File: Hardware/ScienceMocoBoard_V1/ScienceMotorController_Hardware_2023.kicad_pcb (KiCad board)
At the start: 2 copper layers, 231.4 x 127 mm, 136 parts, among them Q1 SI4156DY, Q10 SI4156DY, Q11 SI4156DY, Q12 SI4156DY, Q13 SI4156DY, Q14 SI4156DY, Q15 SI4156DY, Q16 SI4156DY, Q2 SI4156DY, Q3 SI4156DY, Q4 SI4156DY, Q5 SI4156DY, Q6 SI4156DY, Q7 SI4156DY, Q8 SI4156DY, Q9 SI4156DY, U1 IRS2005S, U10 IRS2005S, U11 TM4C129E_Launchpad, U2 IRS2005S, U3 3V3 OKI, U4 TSR_1-2450, U5 IRS2005S, U6 IRS2005S, U7 IRS2005S, U8 IRS2005S, U9 IRS2005S

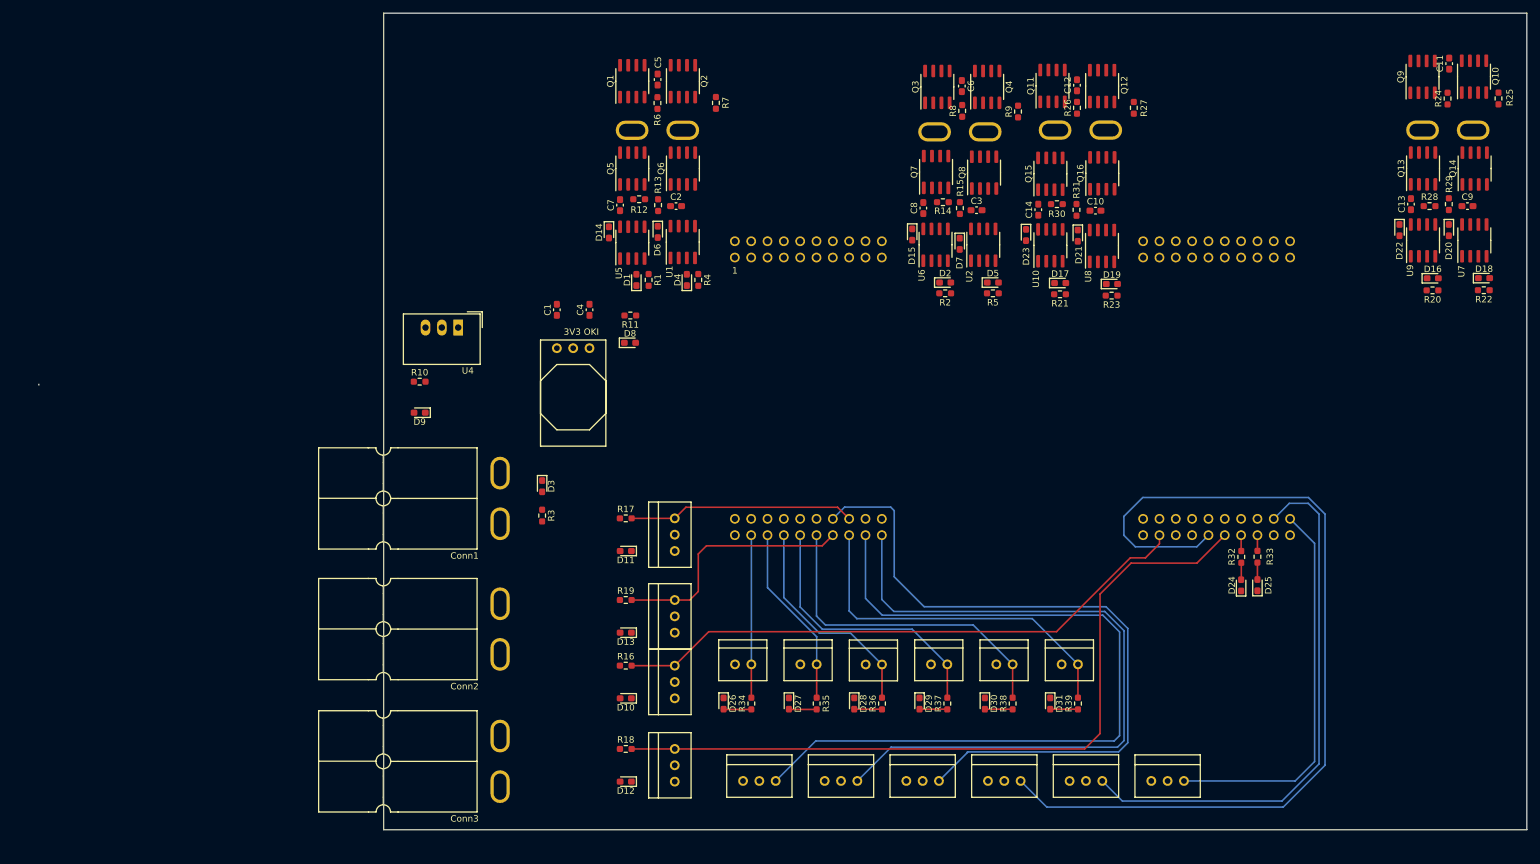
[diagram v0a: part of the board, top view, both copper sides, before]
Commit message: Rearranged Board. Traced Power and One H-Bridge
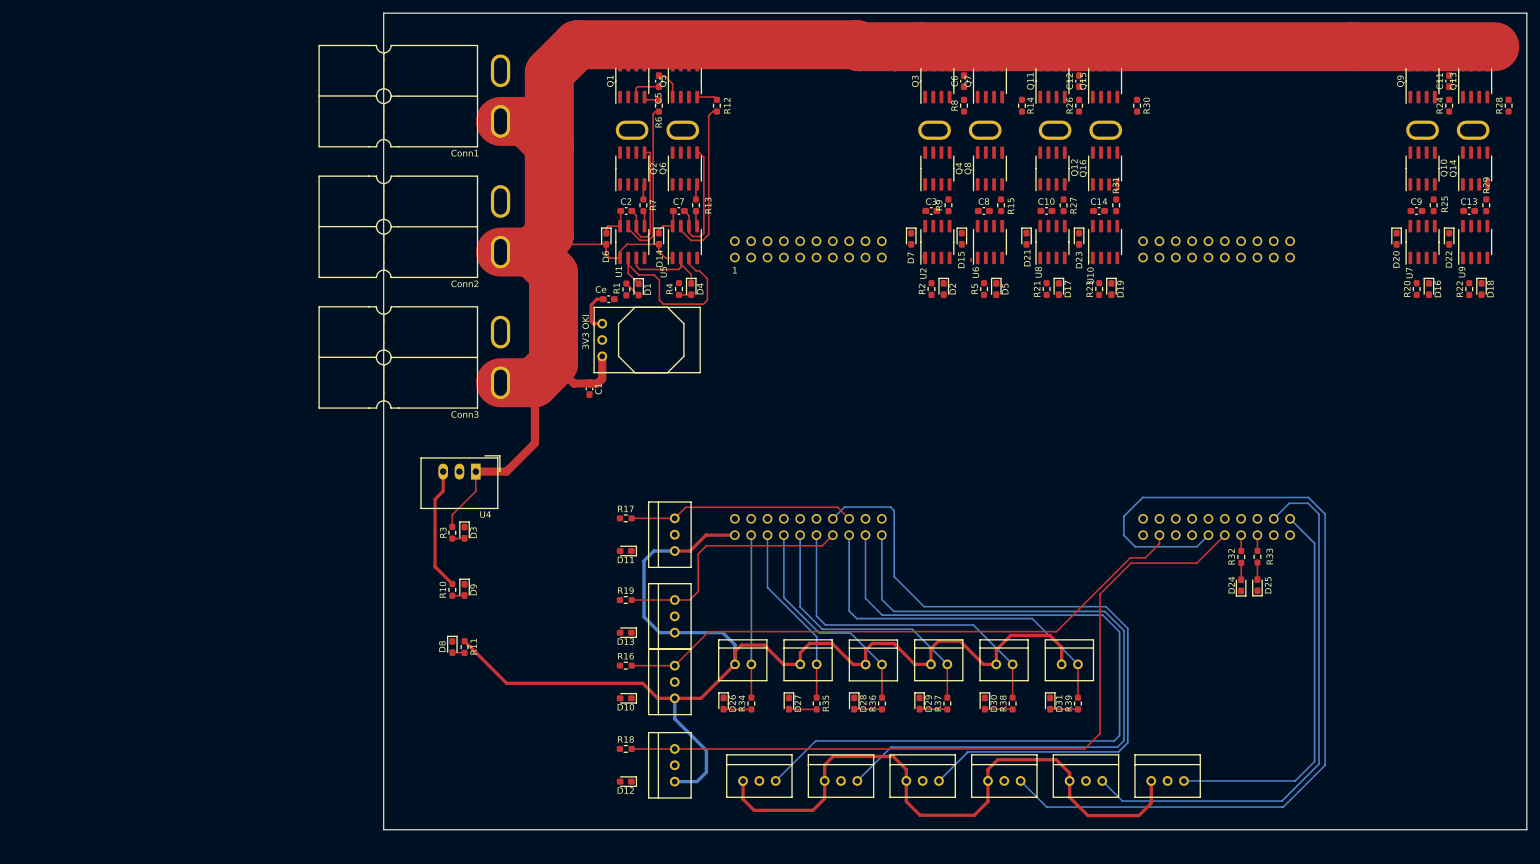
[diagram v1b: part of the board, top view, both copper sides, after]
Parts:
- moved Conn3 62.8 mm to (82.8, 74.9)
- moved Conn2 62.6 mm to (82.8, 54.6)
- moved Conn1 62.6 mm to (82.8, 34.3)
- moved R11 57.6 mm to (76.8, 124.5), turned to 90 degrees
- moved D8 54.8 mm to (74.9, 124.5), turned to -90 degrees
- moved R10 32.8 mm to (74.9, 115.6), turned to 90 degrees
- moved D9 28.4 mm to (76.8, 115.6), turned to -90 degrees
- moved U4 22.6 mm to (78.6, 97.2)
- moved R28 19.9 mm to (239.2, 40.3), turned to 90 degrees
- moved R30 19.8 mm to (181.4, 40.3), turned to 90 degrees
- moved R7 19.5 mm to (104.6, 55.8)
- moved R25 19.4 mm to (227.6, 55.8)
- moved R14 19.4 mm to (163.5, 40.3), turned to 90 degrees
- moved R12 18.9 mm to (116.1, 40.3), turned to 90 degrees
- moved R27 18.7 mm to (170.0, 55.8)
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- renumbered C4 to Ce
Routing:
- net +12V: track 0.00 -> 299.0 mm
- net +3V3: track 0.00 -> 190.6 mm
- net +5V: track 0.36 -> 116.4 mm
- net FWD_PWM_1: track 0.00 -> 30.7 mm
- net Net-(R12-Pad1): track 0.00 -> 26.0 mm
- net Net-(R6-Pad1): track 0.00 -> 25.3 mm
- net /M+: track 0.00 -> 24.7 mm
- net /M-: track 0.00 -> 24.3 mm
- net RVS_PWM_1: track 0.00 -> 14.6 mm
- net Net-(C2-Pad1): track 0.00 -> 5.46 mm
- net Net-(C7-Pad1): track 0.00 -> 5.27 mm
- net Net-(Q5-Pad4): track 0.00 -> 3.25 mm
- net Net-(D1-Pad2): track 0.00 -> 2.65 mm
- net Net-(Q1-Pad4): track 0.00 -> 2.41 mm
- net Net-(R7-Pad1): track 0.00 -> 2.40 mm
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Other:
- board size 231.4 x 127 mm -> 177.8 x 127 mm

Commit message: More tracing. Ground is left.
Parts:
- moved AbsEncode4 1.17 mm to (109.5, 133.6)
- moved D15 0.43 mm to (154.6, 61.0)
- moved C11 0.38 mm to (230.0, 36.8)
- moved C12 0.38 mm to (172.4, 36.8)
- moved C6 0.38 mm to (154.5, 36.8)
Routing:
- net +12V: track 299.0 -> 432.1 mm
- net +5V: track 116.4 -> 205.7 mm
- net RVS_PWM_2: track 0.00 -> 81.7 mm
- net FWD_PWM_2: track 0.00 -> 81.5 mm
- net FWD_PWM_3: track 0.00 -> 77.5 mm
- net /M+: track 24.7 -> 98.6 mm
- net /M-: track 24.3 -> 93.8 mm
- net RVS_PWM_3: track 0.00 -> 62.3 mm, vias 0 -> 2
- net FWD_PWM_4: track 0.00 -> 55.4 mm
- net RVS_PWM_4: track 0.00 -> 53.8 mm, vias 0 -> 2
- net +3V3: track 190.6 -> 232.1 mm
- net RVS_PWM_1: track 14.6 -> 43.5 mm
- net Net-(R28-Pad1): track 0.00 -> 26.2 mm
- net Net-(R14-Pad1): track 0.00 -> 26.1 mm
- net Net-(R30-Pad1): track 0.00 -> 24.9 mm
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- added copper zone on F.Cu, net /M+
- added copper zone on F.Cu, net /M-
- added copper zone on B.Cu, net GND
- added copper zone on F.Cu, net GND

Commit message: Finished layout. BOM is left.
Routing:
- net /M+: track 98.6 -> 249.6 mm, vias 0 -> 4
- net /M-: track 93.8 -> 228.6 mm, vias 0 -> 4
- net +12V: track 432.1 -> 423.8 mm
- net RVS_PWM_2: track 81.7 -> 84.0 mm
- net FWD_PWM_2: track 81.5 -> 79.7 mm
- net GND: track 0.54 -> 2.07 mm, vias 0 -> 21

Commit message: Power Plane Added, New Powerlines, Made Silkscreen Labels
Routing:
- net +12V: track 423.8 -> 274.1 mm
- net +3V3: track 232.1 -> 297.9 mm
- net +5V: track 205.7 -> 206.3 mm
- net GND: vias 21 -> 45
- added copper zone on F.Cu, net +12V
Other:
- board text added: "12V"
- board text added: "3.3V"
- board text added: "5V"

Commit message: Board Smaller, H-Bridges moved
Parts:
- Conn1, Conn2, Conn3, U4: moved to B.Cu
- moved Servo1 294.7 mm to (-174.5, 140.6)
- moved Servo2 294.7 mm to (-161.8, 140.6)
- moved Servo3 294.7 mm to (-149.1, 140.6)
- moved Servo4 294.7 mm to (-136.4, 140.6)
- moved Servo5 294.7 mm to (-123.7, 140.6)
- moved Servo6 294.7 mm to (-111.0, 140.6)
- moved D28 292.7 mm to (-147.3, 201.1)
- moved D29 292.7 mm to (-137.1, 201.1)
- moved LimSwitch1 292.7 mm to (-165.8, 195.0)
- moved LimSwitch2 292.7 mm to (-155.7, 195.0)
- moved LimSwitch3 292.7 mm to (-145.5, 195.0)
- moved R34 292.7 mm to (-163.3, 201.1)
- moved R38 292.7 mm to (-122.7, 201.1)
- moved R39 292.7 mm to (-112.5, 201.1)
- moved D26 292.7 mm to (-167.6, 201.1)
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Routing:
- net +3V3: track 297.9 -> 0.00 mm
- net +12V: track 274.1 -> 0.00 mm
- net /M+: track 249.6 -> 0.00 mm, vias 4 -> 0
- net /M-: track 228.6 -> 0.00 mm, vias 4 -> 0
- net +5V: track 206.3 -> 0.00 mm
- net Servo_4: track 142.0 -> 0.00 mm
- net Servo_1: track 124.0 -> 0.00 mm
- net Encoder_PWM_3: track 118.7 -> 0.00 mm
- net Servo_2: track 110.9 -> 0.00 mm
- net Servo_3: track 110.1 -> 0.00 mm
- net Encoder_PWM_2: track 92.9 -> 0.00 mm
- net Servo_5: track 85.0 -> 0.00 mm
- net RVS_PWM_2: track 84.0 -> 0.00 mm
- net FWD_PWM_2: track 79.7 -> 0.00 mm
- net FWD_PWM_3: track 77.5 -> 0.00 mm
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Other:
- board size 177.8 x 127 mm -> 124.6 x 127 mm
- board text added: "Power LEDS"

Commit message: Refit Stuff onto Board.
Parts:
- moved D26 374.5 mm to (185.1, 75.1), turned to 90 degrees
- moved LimSwitch1 367.2 mm to (183.3, 81.2), turned to 180 degrees
- moved R34 366.4 mm to (180.8, 75.1), turned to -90 degrees
- moved Servo1 359.6 mm to (183.9, 111.8), turned to 180 degrees
- moved D27 355.5 mm to (174.9, 75.1), turned to 90 degrees
- moved LimSwitch2 348.0 mm to (173.2, 81.2), turned to 180 degrees
- moved R35 347.4 mm to (170.6, 75.1), turned to -90 degrees
- moved AbsEncode2 342.9 mm to (180.9, 125.0), turned to 180 degrees
- moved D12 341.2 mm to (180.9, 132.6), turned to -90 degrees
- moved D28 336.5 mm to (164.8, 75.1), turned to 90 degrees
- moved Servo2 334.2 mm to (171.2, 111.8), turned to 180 degrees
- moved R18 331.1 mm to (175.8, 132.6), turned to 90 degrees
- moved LimSwitch3 328.9 mm to (163.0, 81.2), turned to 180 degrees
- moved R36 328.6 mm to (160.5, 75.1), turned to -90 degrees
- moved AbsEncode4 319.5 mm to (169.1, 125.0), turned to 180 degrees
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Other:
- board text added: "E1"
- board text added: "E2"
- board text added: "E3"
- board text added: "E4"
- board text added: "LS1"
- board text added: "LS2"
- board text added: "LS3"
- board text added: "LS4"
- board text added: "LS5"
- board text added: "LS6"
- board text added: "S1"
- board text added: "S2"
- board text added: "S3"
- board text added: "S4"
- board text added: "S5"
- board text added: "S6"

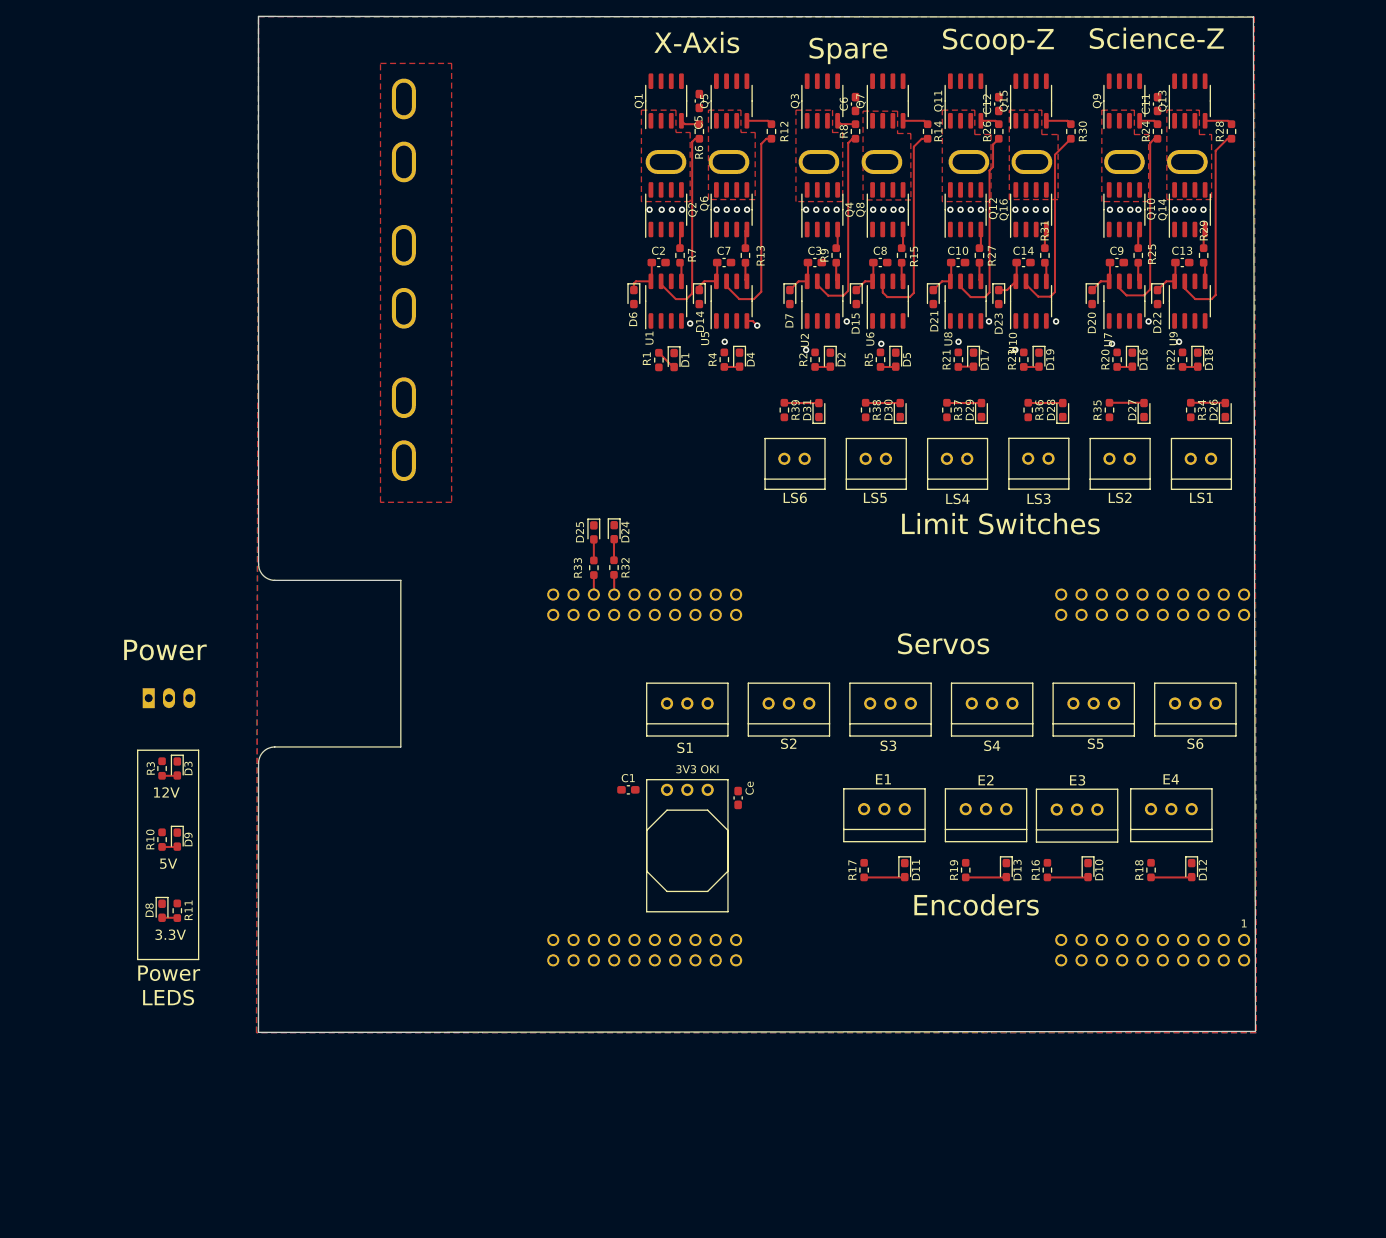
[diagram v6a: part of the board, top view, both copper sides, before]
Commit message: Added Mounting Holes
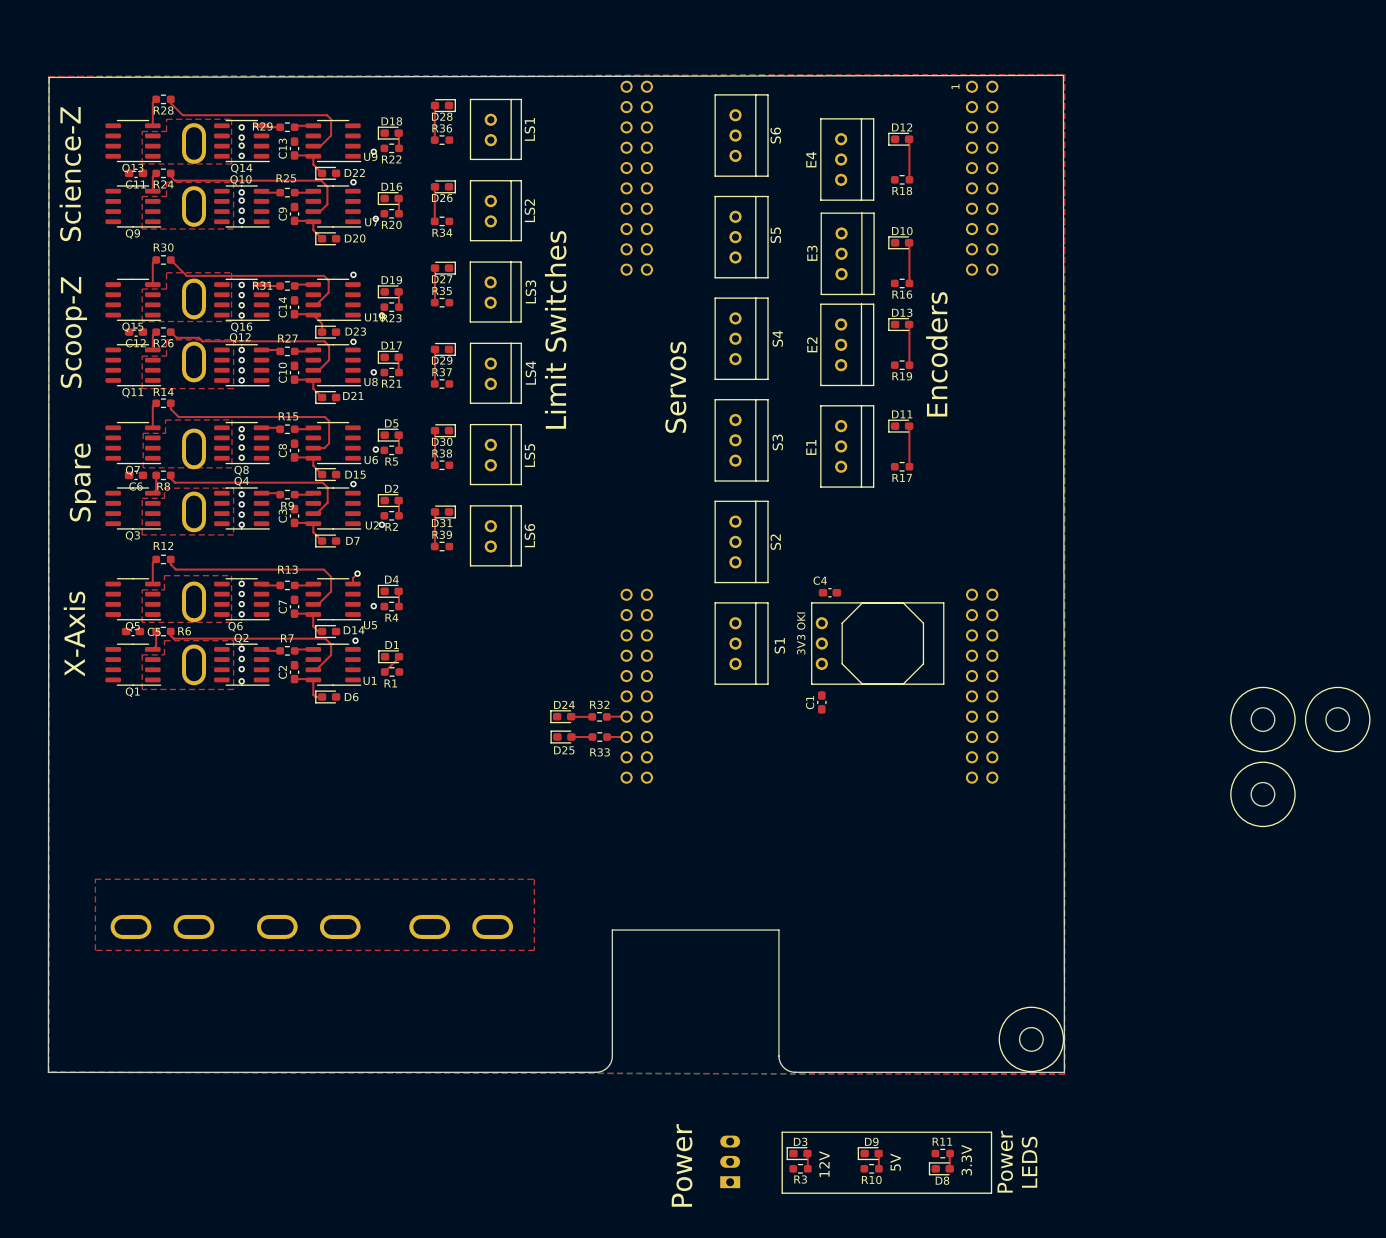
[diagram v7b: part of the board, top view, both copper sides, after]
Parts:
- added V1: Via, MRDT_Drill_Holes:4_40_Hole_Corner, F.Cu at (185.8, 127.1)
- added V2: Via, MRDT_Drill_Holes:4_40_Hole_Corner, F.Cu at (195.2, 117.8)
- added V3: Via, MRDT_Drill_Holes:4_40_Hole_Corner, F.Cu at (156.9, 149.7)
- added V4: Via, MRDT_Drill_Holes:4_40_Hole_Corner, F.Cu at (185.8, 117.8)
- moved R28 133.6 mm to (52.4, 36.2), turned to 180 degrees
- moved Q13 132.2 mm to (48.6, 41.5), turned to 180 degrees
- moved C11 128.0 mm to (48.9, 45.5), turned to 180 degrees
- moved Q9 124.6 mm to (48.6, 49.6), turned to 180 degrees
- moved R24 124.4 mm to (52.4, 45.5), turned to 180 degrees
- moved Q14 118.8 mm to (62.2, 41.5), turned to 180 degrees
- moved R29 115.6 mm to (67.9, 39.7), turned to 180 degrees
- moved Conn6 115.5 mm to (56.6, 50.2), turned to 0 degrees
- moved Q15 115.0 mm to (48.6, 61.3), turned to 180 degrees
- moved R30 114.6 mm to (52.4, 56.3), turned to 180 degrees
- moved C13 111.9 mm to (68.8, 42.4), turned to 90 degrees
- moved C12 111.5 mm to (48.9, 65.3), turned to 180 degrees
- moved Q10 110.3 mm to (62.2, 49.6), turned to 180 degrees
- moved Q11 109.2 mm to (48.6, 69.5), turned to 180 degrees
- moved U9 108.9 mm to (73.6, 41.5), turned to 180 degrees
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- renumbered Ce to C4, D27 to D26, D28 to D27, D26 to D28, LimSwitch2 to LimSwitch1, LimSwitch3 to LimSwitch2, LimSwitch1 to LimSwitch3, R35 to R34, R36 to R35, R34 to R36
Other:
- board size 124.6 x 127 mm -> 127 x 124.6 mm
